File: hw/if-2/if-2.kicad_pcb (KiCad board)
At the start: 4 copper layers, 100 x 130 mm, 200 parts, among them J1 DB25_Socket, J2 PJ-102AH, J3 Conn_02x12_Odd_Even, J4 Conn_01x02, J5 Conn_01x02, Q1 MMBT3904, Q11 MMBT3904, Q12 MMBT3904, Q2 MMBT3904, U10 NCP1117-5.0_SOT223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

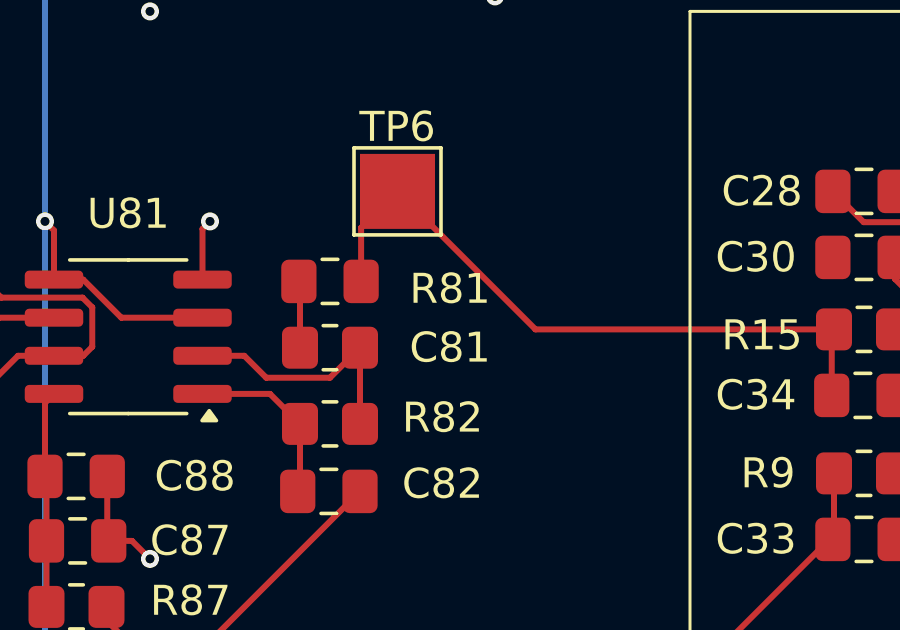
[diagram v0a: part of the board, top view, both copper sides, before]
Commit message: Added audio clip
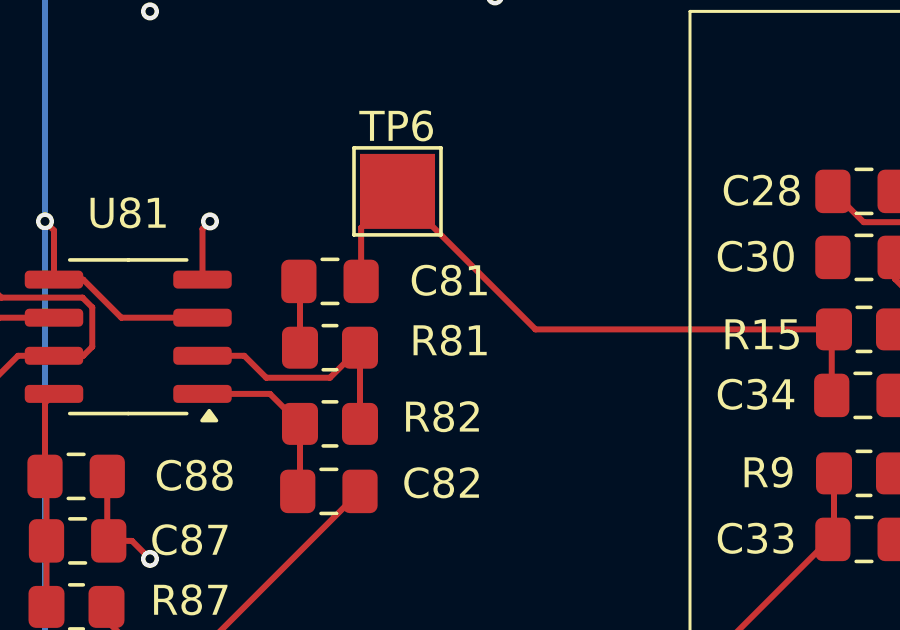
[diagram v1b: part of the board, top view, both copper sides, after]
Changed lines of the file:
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@@
 		(tags "capacitor handsolder")
 		(property "Reference" "C81"
-			(at -4 -2.21 0)
+			(at -4 0 0)
 			(layer "F.SilkS")
 			(effects
@@
 		(tags "resistor handsolder")
 		(property "Reference" "R81"
-			(at 4 -1.96 0)
+			(at 4 -0.21 0)
 			(layer "F.SilkS")
 			(effects
